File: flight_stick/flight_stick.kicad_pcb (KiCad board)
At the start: 2 copper layers, 65.3 x 41.3 mm, 66 parts, among them J1 Load Cell 1, J10 USB_C_Receptacle_USB2.0, J11 Conn_01x05_Pin, J3 Load Cell 5, J5 Load Cell 3, J7 Conn_01x04_Male, J8 Conn_01x05_Pin, J9 Conn_ST_STDC14, Q1 MMS8550, Q3 MMS8550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

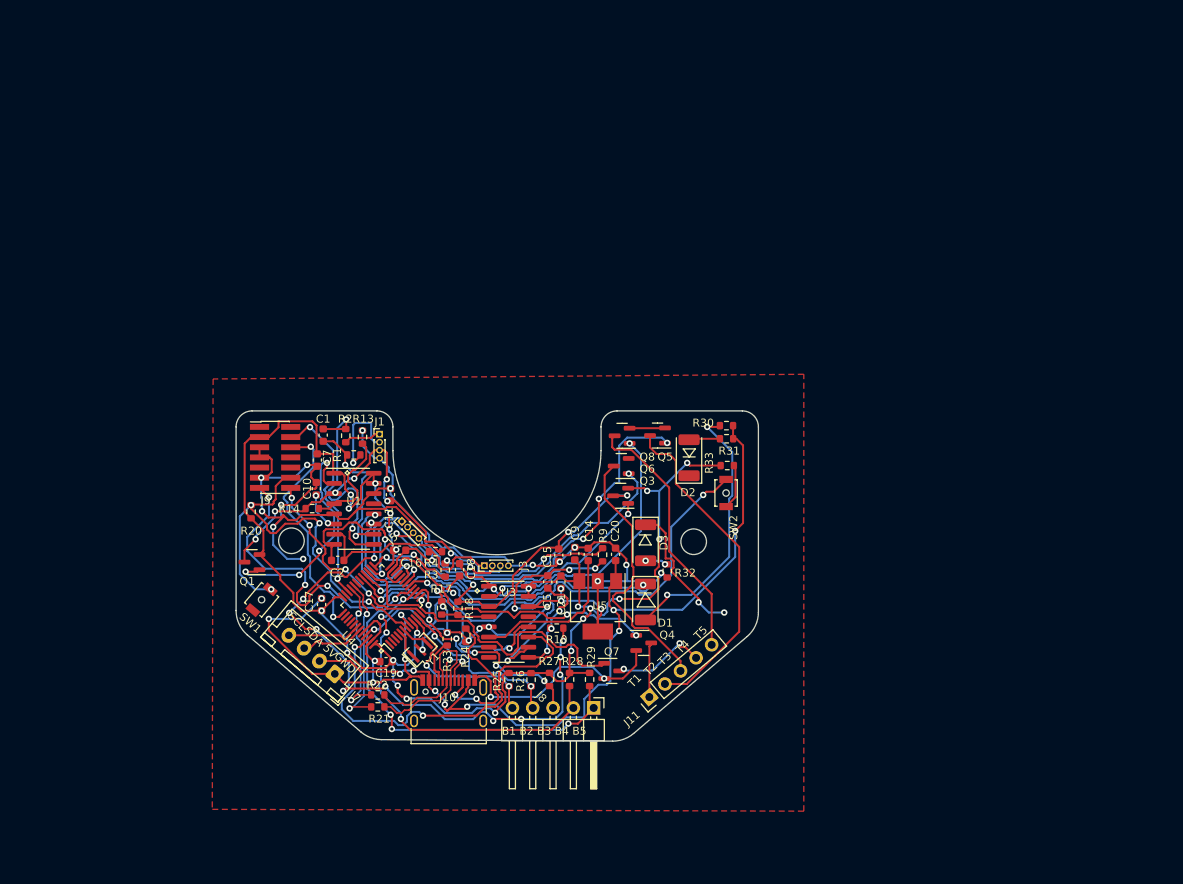
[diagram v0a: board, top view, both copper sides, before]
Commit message: Began Rev4
Changed ADC, reallocated pins, Cleaned up schematic and clear layout
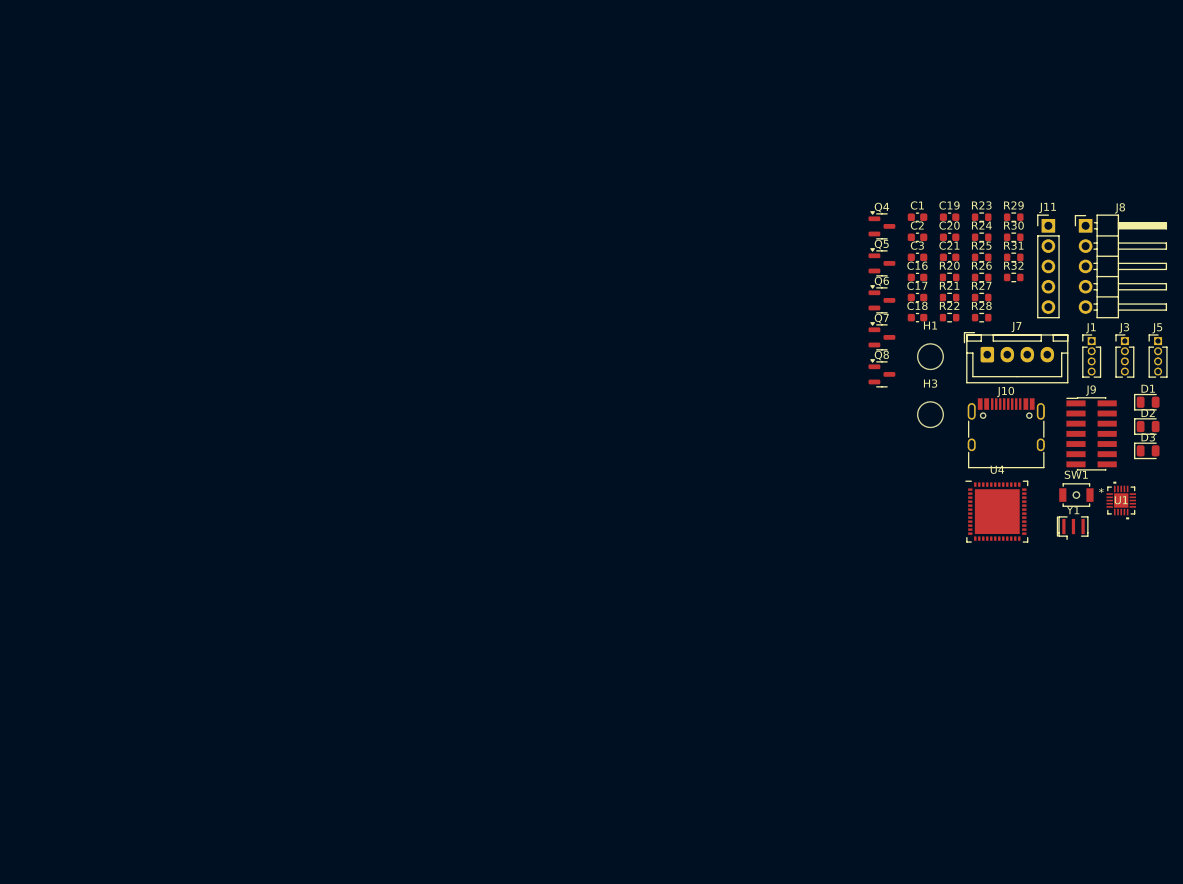
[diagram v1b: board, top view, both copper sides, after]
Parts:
- removed C10, C14, C5: 0.1uF, Capacitor_SMD:C_0603_1608Metric
- removed C11, C15, C7, C9: 10uF, Capacitor_SMD:C_0603_1608Metric
- removed Q1, Q3: MMS8550, Package_TO_SOT_SMD:SOT-23
- removed R1, R10, R2, R3, R33, R4, R9: 100, Resistor_SMD:R_0603_1608Metric
- removed R13, R17: 8.2k, Resistor_SMD:R_0603_1608Metric
- removed R14, R18: 20k, Resistor_SMD:R_0603_1608Metric
- removed SW2: SW_Push, Button_Switch_SMD:SW_SPST_B3U-1000P-B
- removed U3: HX711, Package_SO:SOIC-16_3.9x9.9mm_P1.27mm
- removed U5: LM3940IMP-3.3/NOPB, Package_TO_SOT_SMD:SOT-223
- added C3: C, Capacitor_SMD:C_0603_1608Metric, F.Cu at (187.3, 78.8)
- C1, C2: value 0.1uF -> C
- D1, D2, D3: footprint LED_SMD:LED_2010_5025Metric -> LED_SMD:LED_0805_2012Metric
- J1, J5: footprint Connector_PinHeader_1.00mm:PinHeader_1x04_P1.00mm_Vertical -> Connector_PinHeader_1.27mm:PinHeader_1x04_P1.27mm_Vertical
- J3: value Load Cell 5 -> Load Cell 2; footprint Connector_PinHeader_1.00mm:PinHeader_1x04_P1.00mm_Vertical -> Connector_PinHeader_1.27mm:PinHeader_1x04_P1.27mm_Vertical
- U1: value HX711 -> ADS131M03IRUKR; footprint Package_SO:SOIC-16_3.9x9.9mm_P1.27mm -> ADS131M03 Footprint:QFN_WQFN_RUK_TEX
- U4: value STM32F103C8Tx -> STM32F103C8T6; footprint Package_QFP:LQFP-48_7x7mm_P0.5mm -> STM32F103C8T6_UFQFPN48:QFN-48_EP_7.3x7.3_Pitch0.5mm
- moved SW1 102.7 mm to (207.2, 108.5), turned to 0 degrees
- moved J9 102.1 mm to (209.1, 100.9)
- moved J5 97.2 mm to (217.4, 89.3), turned to 0 degrees
- moved U1 95.9 mm to (212.8, 109.2)
- moved R20 92.1 mm to (191.3, 81.3), turned to 0 degrees
- moved J7 90.8 mm to (196.0, 91.0), turned to 0 degrees
- moved J1 89.8 mm to (209.1, 89.3)
- moved C19 89.7 mm to (191.3, 73.8), turned to 0 degrees
- moved R21 87.9 mm to (191.3, 83.8)
- moved J8 86.1 mm to (208.3, 74.9), turned to 0 degrees
- moved R22 85.6 mm to (191.3, 86.3)
- moved R23 85.1 mm to (195.3, 73.8), turned to 0 degrees
- moved J3 84.8 mm to (213.2, 89.3), turned to 0 degrees
- moved C17 83.8 mm to (187.3, 83.8), turned to 0 degrees
- moved Y1 83.1 mm to (206.8, 112.5), turned to 0 degrees
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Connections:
- C1 pad 1: Net-(U1-IN_{B+}) -> Net-(U1-AIN0N)
- C1 pad 2: Net-(U1-IN_{B-}) -> Net-(U1-AIN0P)
- C2 pad 1: Net-(U1-IN_{A+}) -> Net-(U1-AIN1N)
- C2 pad 2: Net-(U1-IN_{A-}) -> Net-(U1-AIN1P)
- J1 pad 1: /S-_{LC1} -> +3.3V
- J1 pad 2: /S+_{LC1} -> Net-(J1-Pin_2)
- J1 pad 3: /E+_{LC1&2} -> Net-(J1-Pin_3)
- J3 pad 1: /S-_{LC2} -> +3.3V
- J3 pad 2: /S+_{LC2} -> Net-(J3-Pin_2)
- J3 pad 3: /E+_{LC1&2} -> Net-(J3-Pin_3)
- J5 pad 1: /S-_{LC3} -> +3.3V
- J5 pad 2: /S+_{LC3} -> Net-(J5-Pin_2)
- J5 pad 3: /E+_{LC3&4} -> Net-(J5-Pin_3)
- J7 pad 1: GND -> +5V
- J7 pad 2: +5V -> GND
- J8 pad 1: /button5 -> /button1
- J8 pad 2: /button4 -> /button2
- J8 pad 4: /button2 -> /button4
- J8 pad 5: /button1 -> /button5
- R30 pad 1: +5V -> +3.3V
- U1 pad 1: +3.3V -> Net-(U1-AIN0P)
- U1 pad 10: Net-(U1-IN_{B+}) -> /ADC_CS
- U1 pad 11: clk-xforce -> /ADC_DRDY
- U1 pad 12: dout-xforce -> /ADC_SDI
- U1 pad 13: unconnected-(U1-XO-Pad13) -> /ADC_SCK
- U1 pad 14: GND -> /ADC_SDO
- U1 pad 15: +3.3V -> /ADC_MCK
- U1 pad 16: +3.3V -> Net-(U1-CAP)
- U1 pad 2: Net-(Q1-B) -> Net-(U1-AIN0N)
- U1 pad 3: /E+_{LC1&2} -> Net-(U1-AIN1N)
- U1 pad 4: Net-(U1-A_{FB}) -> Net-(U1-AIN1P)
- U1 pad 5: GND -> Net-(U1-AIN2P)
- U1 pad 7: Net-(U1-IN_{A-}) -> unconnected-(U1-NC-Pad7)
- U1 pad 8: Net-(U1-IN_{A+}) -> unconnected-(U1-NC-Pad8)
- U1 pad 9: Net-(U1-IN_{B-}) -> +3.3V
- U4 pad 18: dout-xforce -> unconnected-(U4-PB0-Pad18)
- U4 pad 19: clk-xforce -> unconnected-(U4-PB1-Pad19)
- U4 pad 20: GND -> unconnected-(U4-PB2-Pad20)
- U4 pad 29: Net-(U4-PA8) -> /ADC_MCK
- U4 pad 39: unconnected-(U4-PB3-Pad39) -> /ADC_SCK
- U4 pad 40: dout-shear -> /ADC_SDO
- U4 pad 41: clk-shear -> /ADC_SDI
- U4 pad 42: SCL -> /ADC_CS
- U4 pad 43: SDA -> /ADC_DRDY
- U4 pad 45: dout-yforce -> unconnected-(U4-PB8-Pad45)
- U4 pad 46: clk-yforce -> unconnected-(U4-PB9-Pad46)
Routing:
- net GND: track 295.8 -> 0.00 mm, vias 37 -> 0
- net +3.3V: track 207.8 -> 0.00 mm, vias 23 -> 0
- net +5V: track 102.8 -> 0.00 mm, vias 8 -> 0
- net /S-_{LC3}: track 77.7 -> 0.00 mm, vias 11 -> 0
- net Net-(U4-PA8): track 62.0 -> 0.00 mm, vias 2 -> 0
- net /mcureset: track 53.5 -> 0.00 mm, vias 4 -> 0
- net /Trans2: track 52.9 -> 0.00 mm, vias 4 -> 0
- net /Trans5: track 52.8 -> 0.00 mm, vias 2 -> 0
- net /E+_{LC1&2}: track 52.0 -> 0.00 mm, vias 7 -> 0
- net /button5: track 51.4 -> 0.00 mm, vias 4 -> 0
- net /Trans3: track 51.1 -> 0.00 mm, vias 2 -> 0
- net clk-yforce: track 49.1 -> 0.00 mm, vias 2 -> 0
- net /E+_{LC3&4}: track 48.9 -> 0.00 mm, vias 4 -> 0
- net /button4: track 46.4 -> 0.00 mm, vias 4 -> 0
- net /Programming_{RX}: track 42.4 -> 0.00 mm, vias 4 -> 0
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- removed copper zone on F.Cu, net GND
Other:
- board outline removed
- board text removed: "5V"
- board text removed: "Aryan Ghosh :3"
- board text removed: "B1 B2 B3 B4 B5"
- board text removed: "Flightstick V3 HPVDT"
- board text removed: "GND"
- board text removed: "SCL"
- board text removed: "SDA"
- board text removed: "T1"
- board text removed: "T2"
- board text removed: "T3"
- board text removed: "T4"
- board text removed: "T5"

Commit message: Reviewed Schematic and Assigned Footprints
Changed capacitor and resistor values
Checked all datasheets and made necessary connection changes
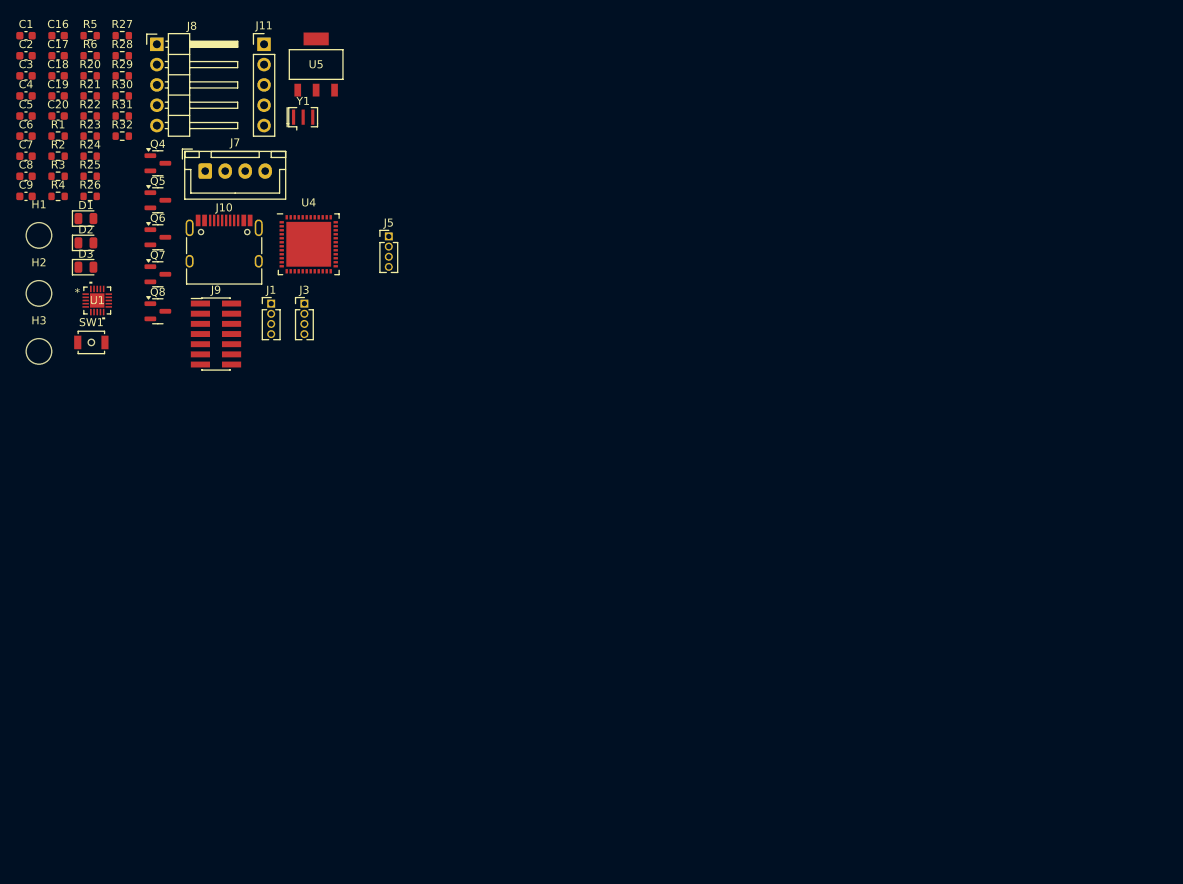
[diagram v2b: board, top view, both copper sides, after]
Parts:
- removed C21: 33uF, Capacitor_SMD:C_0603_1608Metric
- added C4: 220nF, Capacitor_SMD:C_0603_1608Metric, F.Cu at (75.8, 58.6)
- added C5: 100nF, Capacitor_SMD:C_0603_1608Metric, F.Cu at (75.8, 61.1)
- added C6: 100nF, Capacitor_SMD:C_0603_1608Metric, F.Cu at (75.8, 63.6)
- added C7: 10u, Capacitor_SMD:C_0603_1608Metric, F.Cu at (75.8, 66.2)
- added C8: 10u, Capacitor_SMD:C_0603_1608Metric, F.Cu at (75.8, 68.7)
- added C9: 10u, Capacitor_SMD:C_0603_1608Metric, F.Cu at (75.8, 71.2)
- added H2: MountingHole, MountingHole:MountingHole_3.2mm_M3_ISO7380, F.Cu at (77.5, 83.3)
- added R1: 1k, Resistor_SMD:R_0603_1608Metric, F.Cu at (79.9, 63.6)
- added R2: 1k, Resistor_SMD:R_0603_1608Metric, F.Cu at (79.9, 66.2)
- added R3: 1k, Resistor_SMD:R_0603_1608Metric, F.Cu at (79.9, 68.7)
- added R4: 1k, Resistor_SMD:R_0603_1608Metric, F.Cu at (79.9, 71.2)
- added R5: 1k, Resistor_SMD:R_0603_1608Metric, F.Cu at (83.9, 51.1)
- added R6: 1k, Resistor_SMD:R_0603_1608Metric, F.Cu at (83.9, 53.6)
- added U5: LM3940IMP-3.3/NOPB, LFH_Voltagereg:MP04A, F.Cu at (112.1, 54.7)
- C1: value C -> 100nF
- C2, C3: value C -> 100n
- R31: value 100 -> 300
- moved D1 134.8 mm to (83.3, 74.0)
- moved D2 134.8 mm to (83.3, 77.0)
- moved D3 134.8 mm to (83.3, 80.0)
- moved U1 130.4 mm to (84.8, 84.2)
- moved SW1 124.6 mm to (84.0, 89.4)
- moved J8 118.3 mm to (92.2, 52.2)
- moved C1 113.7 mm to (75.8, 51.1)
- moved C2 113.7 mm to (75.8, 53.6)
- moved C3 113.7 mm to (75.8, 56.1)
- moved R29 112.8 mm to (87.9, 56.1)
- moved R30 112.8 mm to (87.9, 58.6)
- moved R31 112.8 mm to (87.9, 61.1)
- moved R32 112.8 mm to (87.9, 63.6)
- moved C20 112.5 mm to (79.9, 61.1)
- moved H1 112.5 mm to (77.5, 76.1)
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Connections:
- J7 pad 3: SDA -> /SCL
- J7 pad 4: SCL -> /SDA
- U4 pad 45: unconnected-(U4-PB8-Pad45) -> /SCL
- U4 pad 46: unconnected-(U4-PB9-Pad46) -> /SDA

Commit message: Began Layout
Started Layout no routing
Added RGB LED
Changed footprints
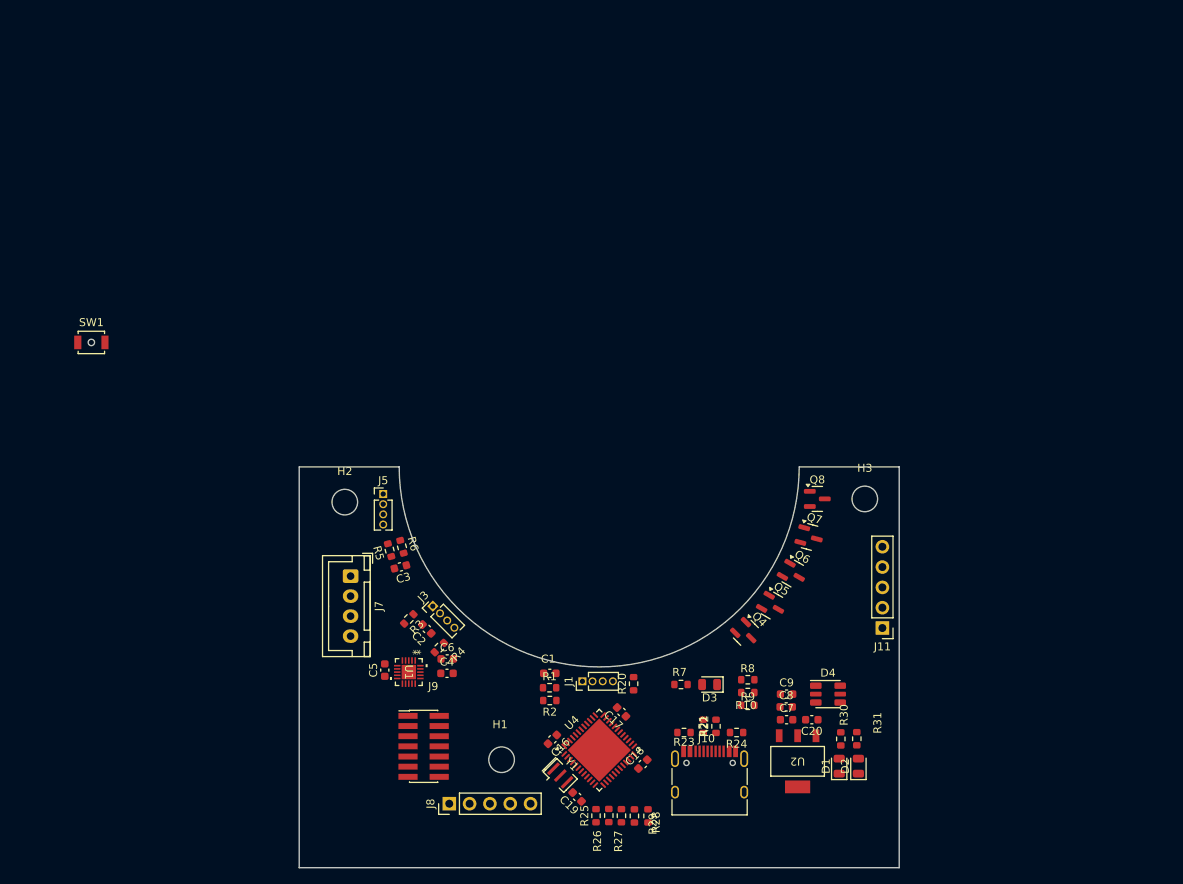
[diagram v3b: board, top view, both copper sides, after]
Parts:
- removed R32: 100, Resistor_SMD:R_0603_1608Metric
- removed U5: LM3940IMP-3.3/NOPB, LFH_Voltagereg:MP04A
- added D4: SMLVN6RGB, LED_SMD:LED_ROHM_SMLVN6, F.Cu at (176.1, 133.4)
- added R10: 50, Resistor_SMD:R_0603_1608Metric, F.Cu at (166.1, 134.8)
- added R7: 100, Resistor_SMD:R_0603_1608Metric, F.Cu at (157.7, 132.2)
- added R8: 50, Resistor_SMD:R_0603_1608Metric, F.Cu at (166.1, 131.6)
- added R9: 100, Resistor_SMD:R_0603_1608Metric, F.Cu at (166.1, 133.2)
- added U2: LM3940IMP-3.3/NOPB, flight_stick_footprints:MP04A, F.Cu at (172.3, 141.8)
- C4: value 220nF -> 220n
- C5, C6: value 100nF -> 100n
- J8: footprint Connector_PinHeader_2.54mm:PinHeader_1x05_P2.54mm_Horizontal -> Connector_PinHeader_2.54mm:PinHeader_1x05_P2.54mm_Vertical
- U1: value ADS131M03IRUKR -> ADS131M03IRUKx; footprint ADS131M03 Footprint:QFN_WQFN_RUK_TEX -> flight_stick_footprints:QFN_WQFN_RUK_TEX
- U4: value STM32F103C8T6 -> STM32F103CBU6; footprint STM32F103C8T6_UFQFPN48:QFN-48_EP_7.3x7.3_Pitch0.5mm -> Package_DFN_QFN:QFN-48-1EP_7x7mm_P0.5mm_EP5.6x5.6mm
- Y1: value 8Mhz -> 8M
- moved C20 120.7 mm to (174.1, 136.6), turned to 180 degrees
- moved R30 120.5 mm to (177.7, 139.0), turned to -90 degrees
- moved R31 120.4 mm to (179.7, 139.0), turned to -90 degrees
- moved C7 118.3 mm to (170.9, 136.6)
- moved D2 116.6 mm to (179.9, 142.4), turned to 90 degrees
- moved D1 116.4 mm to (177.5, 142.4), turned to 90 degrees
- moved C8 115.9 mm to (170.9, 135.0)
- moved R27 115.8 mm to (150.3, 148.6), turned to 90 degrees
- moved R28 114.6 mm to (151.9, 148.6), turned to 90 degrees
- moved C9 113.6 mm to (170.9, 133.4)
- moved R29 113.5 mm to (153.6, 148.6), turned to 90 degrees
- moved C18 112.9 mm to (153.0, 142.1), turned to 45 degrees
- moved R21 109.9 mm to (160.5, 137.4), turned to 90 degrees
- moved R22 109.3 mm to (162.1, 137.4), turned to 90 degrees
- moved C19 109.0 mm to (144.7, 146.3), turned to 135 degrees
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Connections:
- U4 pad 18: unconnected-(U4-PB0-Pad18) -> /StatusLED_{B}
- U4 pad 19: unconnected-(U4-PB1-Pad19) -> /StatusLED_{R}
- U4 pad 20: unconnected-(U4-PB2-Pad20) -> /StatusLED_{G}
- U4 pad 49: (no net) -> GND
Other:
- board outline added: 75 x 50.1 mm

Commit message: Finalized Component Placement
Finished Component Placement
Changed switch
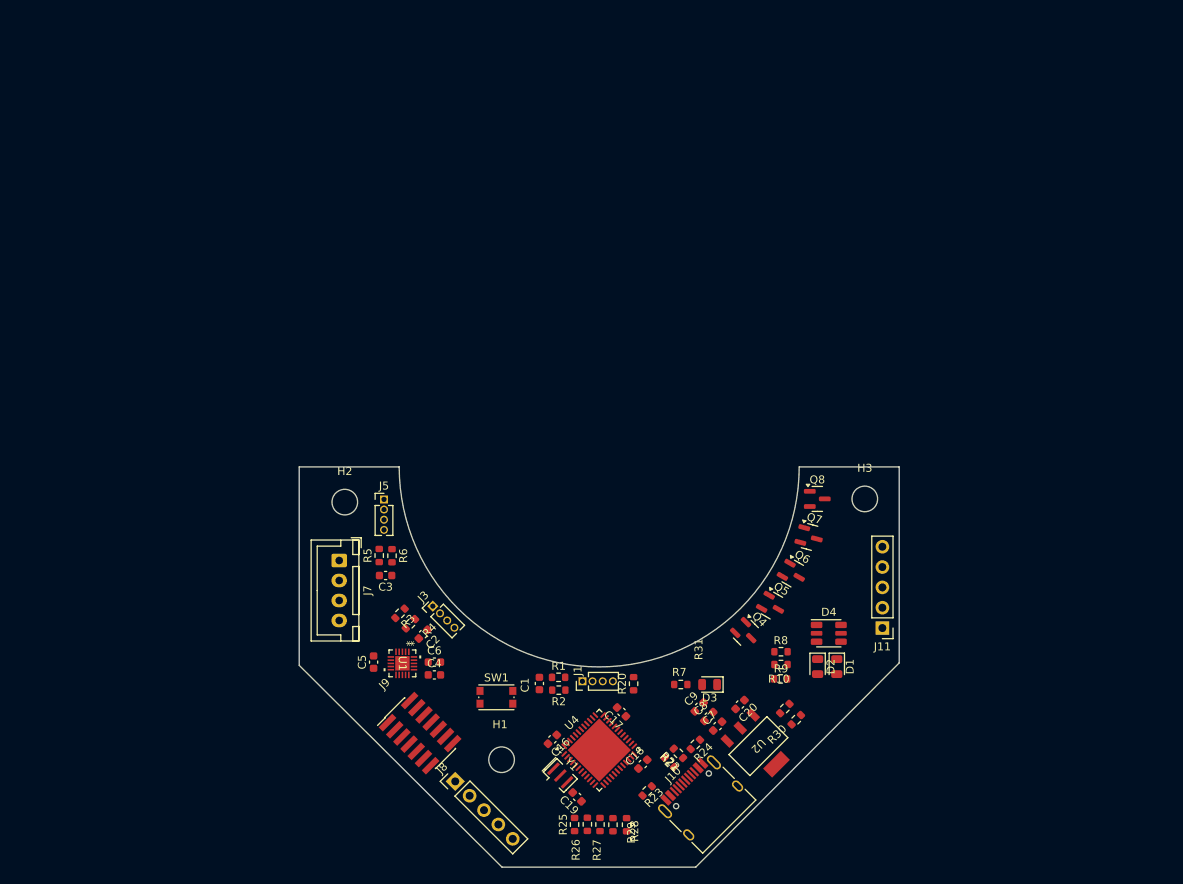
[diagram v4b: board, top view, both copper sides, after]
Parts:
- SW1: footprint Button_Switch_SMD:SW_SPST_B3U-1000P-B -> Button_Switch_SMD:SW_Push_1P1T_NO_CK_KMR2
- moved SW1 67.3 mm to (134.7, 133.8)
- moved D2 13.4 mm to (174.8, 130.0), turned to -90 degrees
- moved D1 12.4 mm to (177.2, 130.0), turned to -90 degrees
- moved C9 11.0 mm to (160.0, 135.0), turned to 45 degrees
- moved R31 9.76 mm to (170.7, 135.2), turned to 45 degrees
- moved C8 9.75 mm to (161.2, 136.2), turned to 45 degrees
- moved C20 9.17 mm to (165.1, 134.7), turned to -135 degrees
- moved C7 8.66 mm to (162.3, 137.4), turned to 45 degrees
- moved R23 8.63 mm to (153.5, 145.5), turned to 45 degrees
- moved D4 7.60 mm to (176.2, 125.8)
- moved R21 6.18 mm to (156.3, 141.9), turned to 135 degrees
- moved R30 6.06 mm to (172.1, 136.6), turned to 45 degrees
- moved R22 5.79 mm to (157.4, 140.8), turned to 135 degrees
- moved R8 5.43 mm to (170.2, 128.1)
- moved R9 5.43 mm to (170.2, 129.7)
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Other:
- board size 75 x 50.1 mm -> 75 x 50 mm
